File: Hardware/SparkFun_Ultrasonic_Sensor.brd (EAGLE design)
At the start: 45 x 21.5 mm, 60 parts, among them J4 Vertical Qwiic Connector, J6 Vertical Qwiic Connector, Q1 600mA/40V, U5 ULTRASONIC_SENSOR_TRANSMITTER, U6 LMV324, U7 STM8L051F3, U8 SP3232EB, U9 ULTRASONIC_SENSOR_RECEIVER

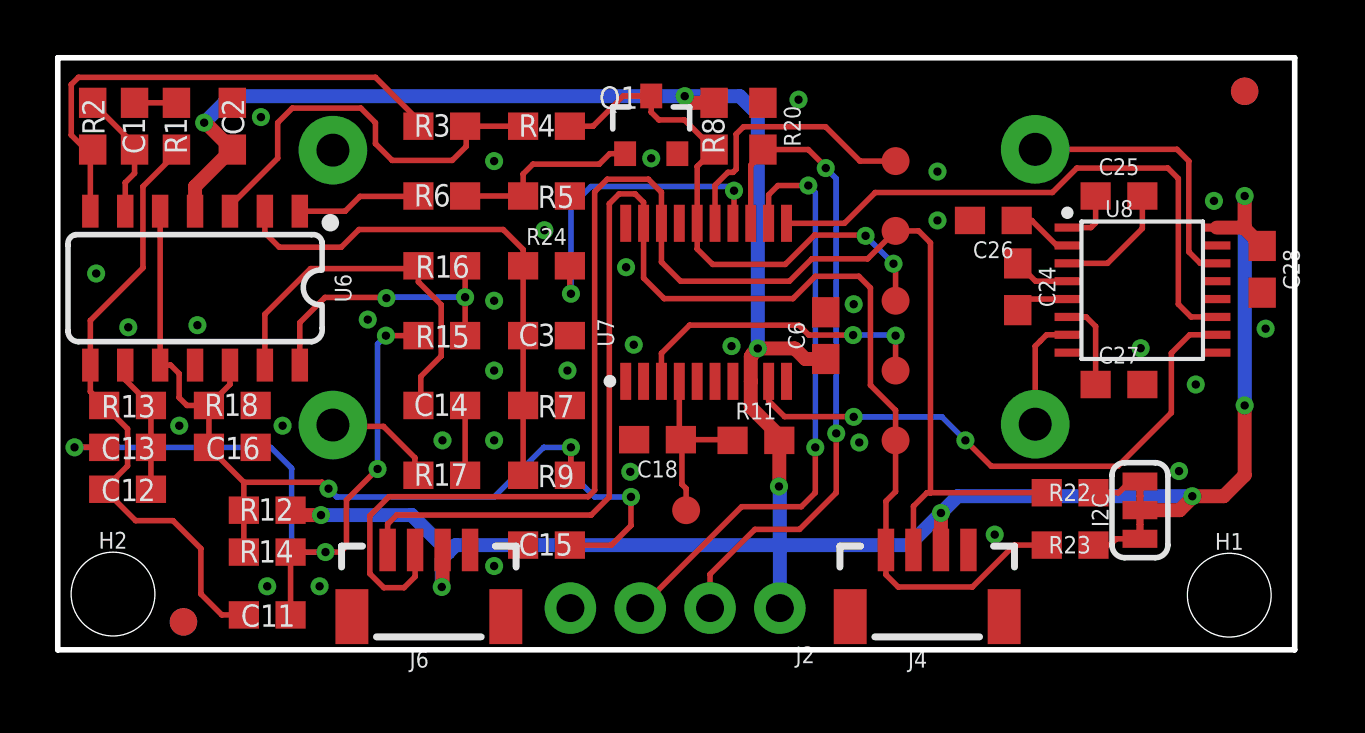
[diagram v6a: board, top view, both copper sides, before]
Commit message: Adds more vias
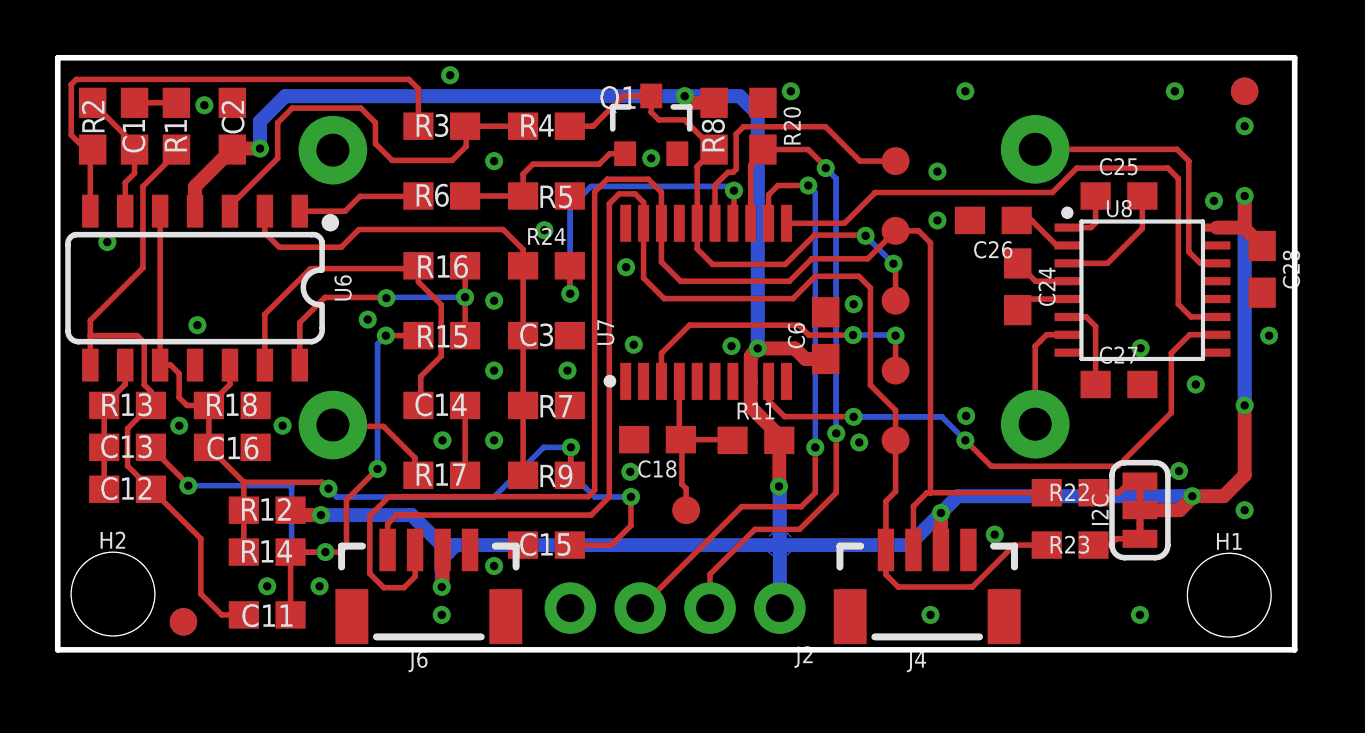
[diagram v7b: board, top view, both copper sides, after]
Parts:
- turned C12 to 0 degrees
- turned C13 to 0 degrees
- turned R13 to 0 degrees
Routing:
- net N$12: track 27.1 -> 22.9 mm
- net N$10: track 22.5 -> 23.8 mm
- net N$1: track 18.7 -> 19.3 mm
- added copper zone on layer 16, net 3.3V
